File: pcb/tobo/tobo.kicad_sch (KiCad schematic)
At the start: 96 parts, among them J1 Molex 538-54548-2272, J2 Conn_01x02_Pin, J4 Molex 538-54548-2472, J5 Conn_01x09_Pin, J6 Conn_01x09_Pin, J7 Conn_01x09_Pin, J8 Hroparts Elec TYPE-C-31-M-12, U1 TS5A23167, U10 5015, U11 5015, U12 5015, U13 5015, U14 CH340E, U15 5015, U2 ATmega328P-A, U3 TS5A23167, U4 TS5A23167, U5 TS5A23167, U6 5015, U7 5015, U8 5015, U9 5015, X1 TestPoint, X2 TestPoint, X7 TestPoint, Y4 TestPoint

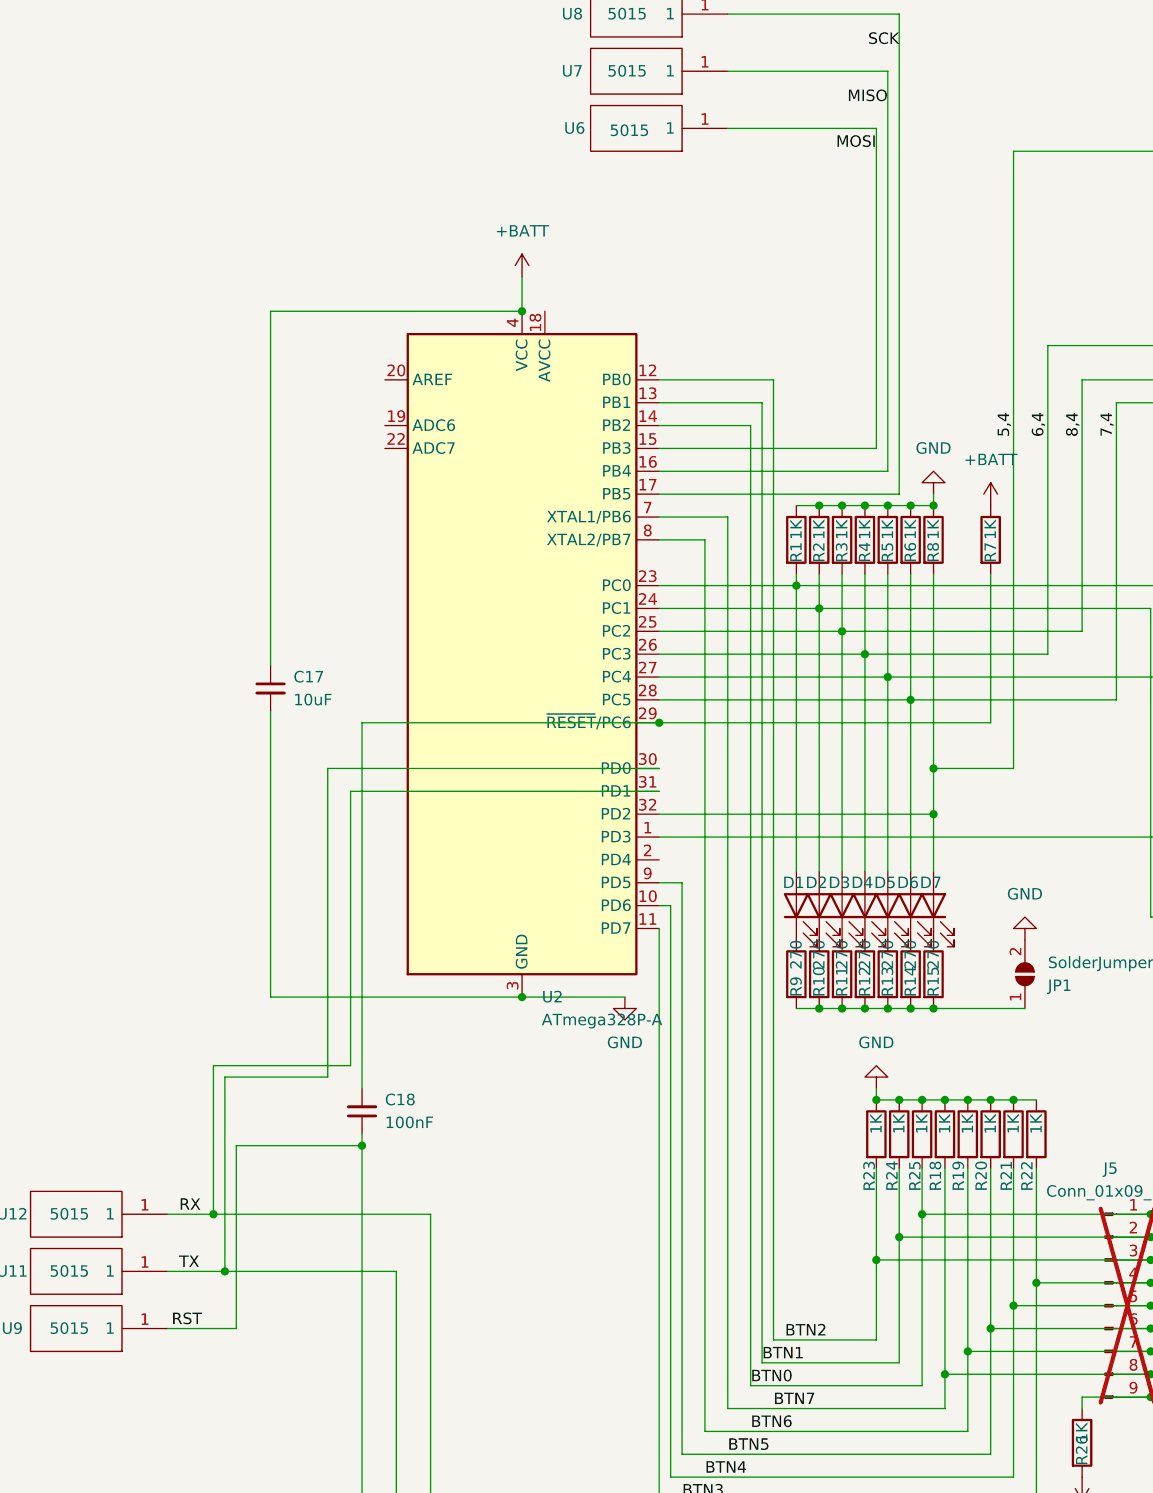
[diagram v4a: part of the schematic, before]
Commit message: Separate DTR from RST pin. They are different.
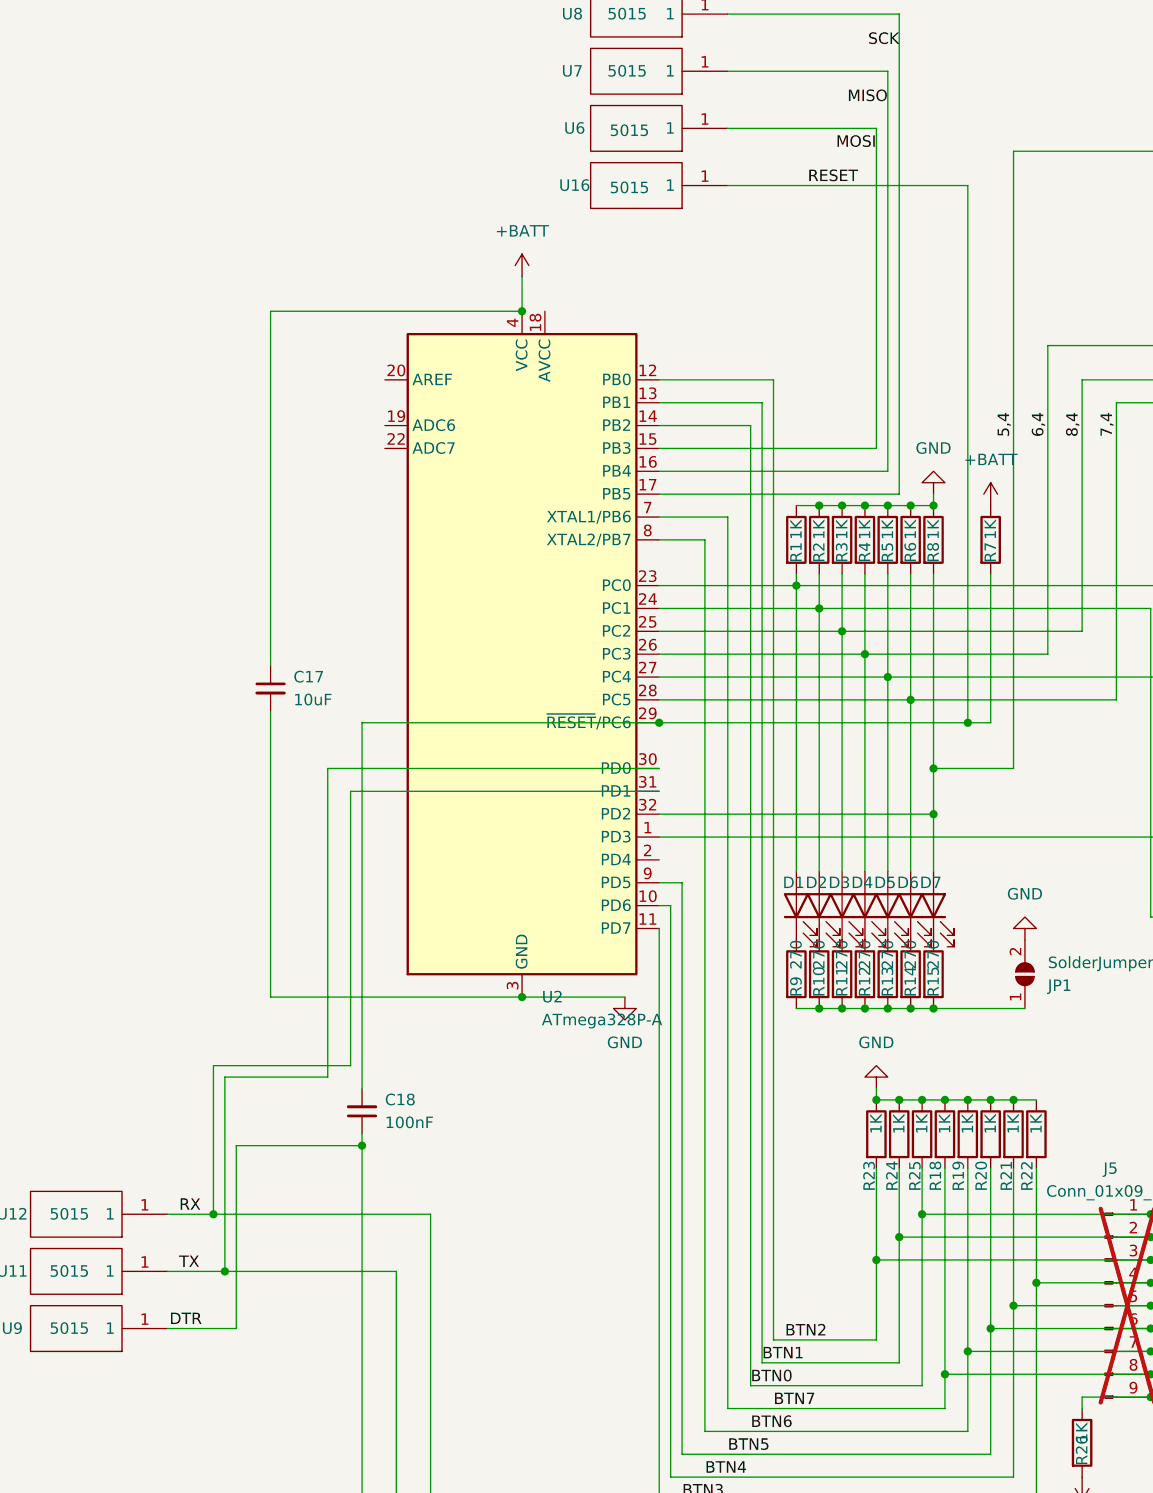
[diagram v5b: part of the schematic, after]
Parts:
- added U16: 5015, tobo-footprints:5015, symbol tobo-components:5015
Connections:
- net RESET: now reaches C18.2, R7.2, U2.29 (~{RESET}/PC6)
- net RESET: now also U16.1
- net RST renamed DTR
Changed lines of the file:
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@@
 	)
 	(junction
+		(at 124.46 110.49)
+		(diameter 0)
+		(color 0 0 0 0)
+	)
+	(junction
 		(at 189.23 81.28)
 		(diameter 0)
@@
 	(wire
 		(pts
+			(xy 124.46 110.49) (xy 124.46 50.8)
+		)
+		(stroke
+			(width 0)
+			(type default)
+		)
+	)
+	(wire
+		(pts
 			(xy 101.6 74.93) (xy 101.6 181.61)
 		)
@@
 	(wire
 		(pts
-			(xy 90.17 110.49) (xy 127 110.49)
+			(xy 90.17 110.49) (xy 124.46 110.49)
 		)
 		(stroke
@@
 	(wire
 		(pts
+			(xy 124.46 110.49) (xy 127 110.49)
+		)
+		(stroke
+			(width 0)
+			(type default)
+		)
+	)
+	(wire
+		(pts
 			(xy 223.52 102.87) (xy 171.45 102.87)
 		)
@@
 	(wire
 		(pts
+			(xy 124.46 50.8) (xy 97.79 50.8)
+		)
+		(stroke
+			(width 0)
+			(type default)
+		)
+	)
+	(wire
+		(pts
 			(xy 115.57 204.47) (xy 111.76 204.47)
 		)
@@
 		)
 	)
-	(label "RST"
+	(label "DTR"
 		(at 39.37 177.8 180)
 		(fields_autoplaced yes)
@@
 		)
 	)
+	(label "RESET"
+		(at 106.68 50.8 0)
+		(fields_autoplaced yes)
+		(effects
+			(font
+				(size 1.27 1.27)
+			)
+			(justify left bottom)
+		)
+	)
 	(label "RX"
 		(at 36.83 165.1 0)
@@
 					(unit 1)
 				)
+			)
+		)
+	)
+	(symbol
+		(lib_id "tobo-components:5015")
+		(at 97.79 50.8 180)
+		(unit 1)
+		(exclude_from_sim no)
+		(in_bom yes)
+		(on_board yes)
+		(dnp no)
+		(property "Reference" "U16"
+			(at 80.772 50.8 0)
+			(effects
+				(font
+					(size 1.27 1.27)
+				)
+			)
+		)
+		(property "Value" "5015"
+			(at 86.868 51.054 0)
+			(effects
+				(font
+					(size 1.27 1.27)
+				)
+			)
+		)
+		(property "Footprint" "tobo-footprints:5015"
+			(at 81.28 53.34 0)
+			(effects
+				(font
+					(size 1.27 1.27)
+				)
+				(justify left)
+				(hide yes)
+			)
+		)
+		(property "Datasheet" "http://www.keyelco.com/product-pdf.cfm?p=1353"
+			(at 81.28 50.8 0)
+			(effects
+				(font
+					(size 1.27 1.27)
+				)
+				(justify left)
+				(hide yes)
+			)
+		)
+		(property "Description" "Conn Test Point 1 POS Solder ST SMD 1 Port T/R"
+			(at 81.28 48.26 0)
+			(effects
+				(font
+					(size 1.27 1.27)
+				)
+				(justify left)
+				(hide yes)
+			)
+		)
+		(property "Height" "1.52"
+			(at 81.28 45.72 0)
+			(effects
+				(font
+					(size 1.27 1.27)
+				)
+				(justify left)
+				(hide yes)
+			)
+		)
+		(property "Manufacturer_Name" "Keystone Electronics"
+			(at 81.28 43.18 0)
+			(effects
+				(font
+					(size 1.27 1.27)
+				)
+				(justify left)
+				(hide yes)
+			)
+		)
+		(property "Manufacturer_Part_Number" "5015"
+			(at 81.28 40.64 0)
+			(effects
+				(font
+					(size 1.27 1.27)
+				)
+				(justify left)
+				(hide yes)
+			)
+		)
+		(property "Mouser Part Number" "534-5015"
+			(at 81.28 38.1 0)
+			(effects
+				(font
+					(size 1.27 1.27)
+				)
+				(justify left)
+				(hide yes)
+			)
+		)
+		(property "Mouser Price/Stock" "https://www.mouser.co.uk/ProductDetail/Keystone-Electronics/5015?qs=qOqV1E1P08ShW56PtUq2FA%3D%3D"
+			(at 81.28 35.56 0)
+			(effects
+				(font
+					(size 1.27 1.27)
+				)
+				(justify left)
+				(hide yes)
+			)
+		)
+		(property "Arrow Part Number" "5015"
+			(at 81.28 33.02 0)
+			(effects
+				(font
+					(size 1.27 1.27)
+				)
+				(justify left)
+				(hide yes)
+			)
+		)
+		(property "Arrow Price/Stock" "https://www.arrow.com/en/products/5015/keystone-electronics?utm_currency=USD&region=europe"
+			(at 81.28 30.48 0)
+			(effects
+				(font
+					(size 1.27 1.27)
+				)
+				(justify left)
+				(hide yes)
+			)
+		)
+		(pin "1"
+		)
+		(instances
+			(project "tobo"
+				(path "/ce2fc4a9-618f-4cc1-898a-224ffa79d770"
+					(reference "U16")
+					(unit 1)
+				)

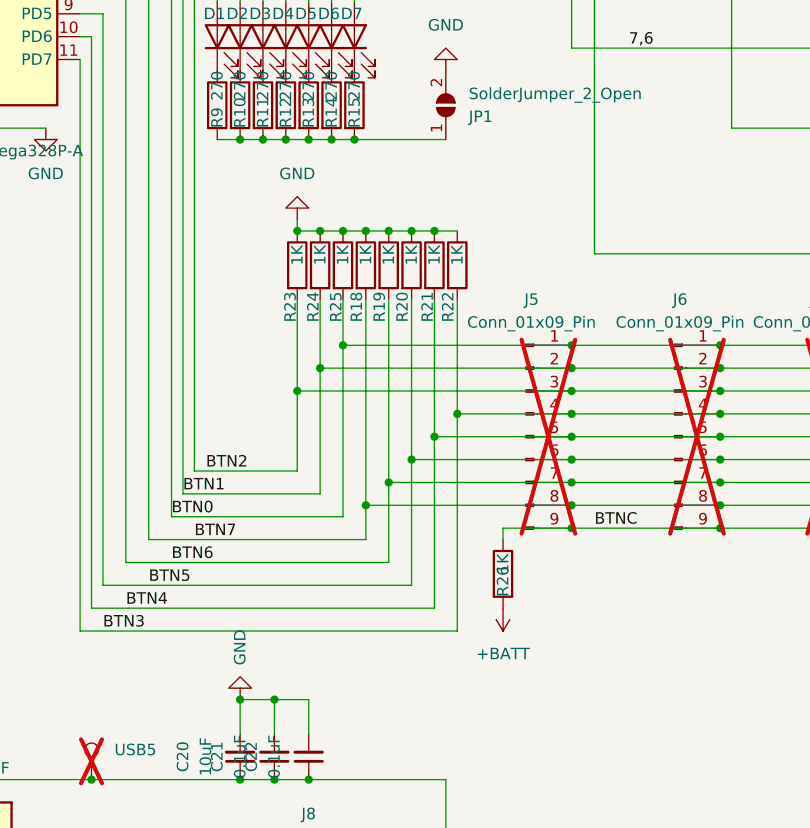
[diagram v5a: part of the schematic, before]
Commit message: Internal pull-ups for the buttons. May as well.
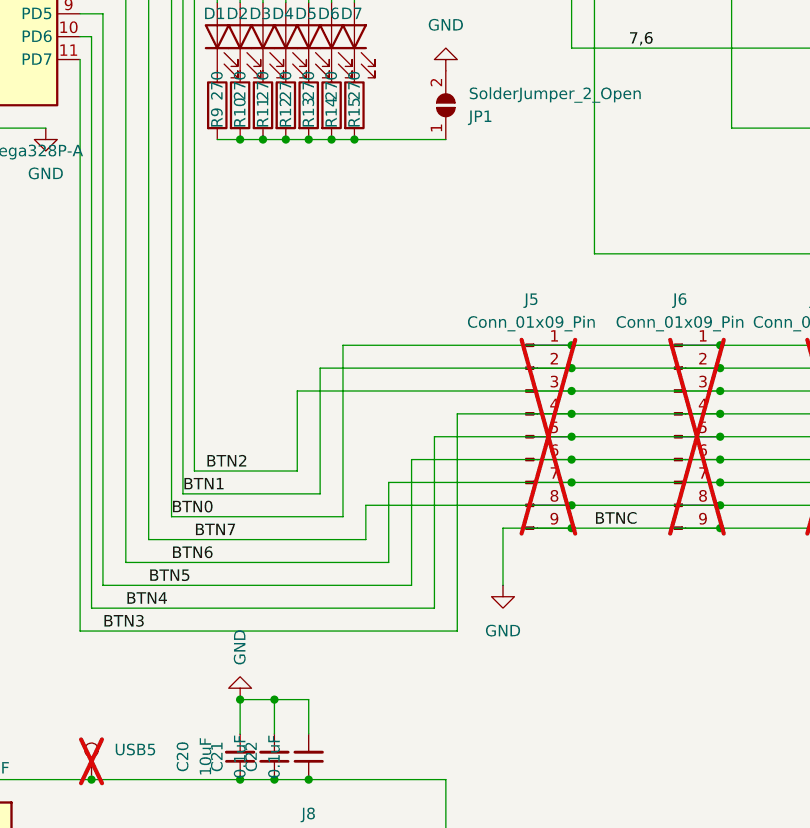
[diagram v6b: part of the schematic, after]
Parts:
- removed R18, R19, R20, R21, R22, R23, R24, R25, R26: 1K, Resistor_SMD:R_0201_0603Metric, symbol Device:R
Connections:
- net BTNC is gone; now on net GND: J5.9 (Pin_9), J6.9 (Pin_9), J7.9 (Pin_9), S1.1 (COM_1), S1.3 (COM_2), S2.1 (COM_1), S2.3 (COM_2), S3.1 (COM_1), S3.3 (COM_2), S4.1 (COM_1), S4.3 (COM_2), S5.1 (COM_1), S5.3 (COM_2)

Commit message: PCB and documentation tweaks
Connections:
- net X1: now reaches J1.11 (X1)
- net X1: now also C7.2, C8.1, J4.13 (X1)
- net X2: now reaches J1.12 (X2)
- net X2: now also C13.1, C14.1, C5.1, C6.2, C9.2, J4.14 (X2), U4.2 (COM1), U4.6 (COM2), U5.6 (COM2), X7.1
- net X3: now reaches J1.13 (X3)
- net X3: now also C1.2, C2.1, J4.15 (X3)
- net X4: now reaches J1.14 (X4)
- net X4: now also C3.1, C4.2, J4.16 (X4), X1.1
- net 5,4 renamed 3,4
- net 6,4 renamed 4,4
- net 7,4 renamed 2,4
- net 7,5 renamed 2,5
- net 7,6 renamed 2,6
- net 7,7 renamed 2,7
- net 8,4 renamed 1,4
- removed net X5: C1.2, C2.1, J1.17 (X5), J4.19 (X5)
- removed net X6: C3.1, C4.2, J1.18 (X6), J4.20 (X6), X1.1
- removed net X7: C13.1, C14.1, C5.1, C6.2, C9.2, J1.16 (X7), J4.18 (X7), U4.2 (COM1), U4.6 (COM2), U5.6 (COM2), X7.1
- removed net X8: C7.2, C8.1, J1.15 (X8), J4.17 (X8)
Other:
- moved on the sheet: X1

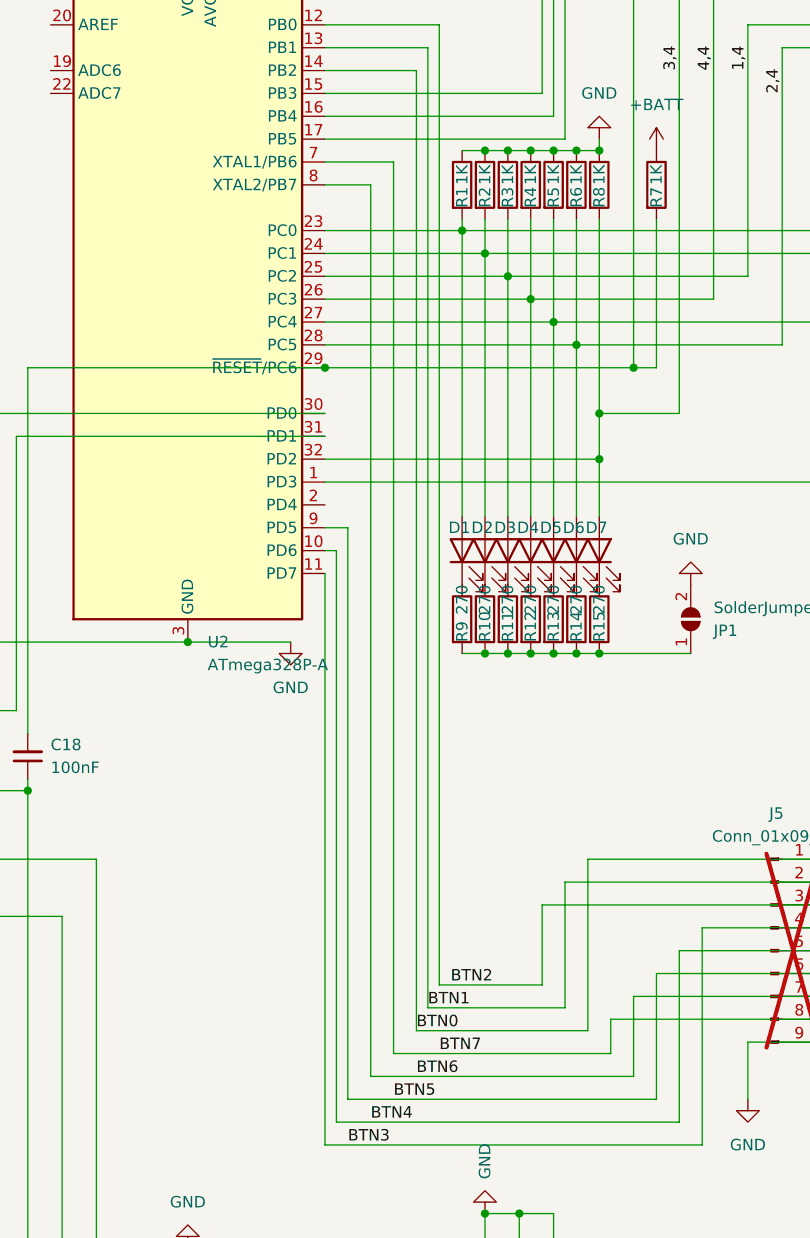
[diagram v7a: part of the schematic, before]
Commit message: Swapped some GPIO to avoid PCINT problems
This lead to a tasty basket weave of traces under the MCU, but that's
fine I guess.

The only reason this change was "necessary" is because regular arduino
doesn't expose gpio on the crystal pins. Therefore the PCINT libraries
don't seem to support enabling the pin change interrupt on those pins.

It was neat to have them as buttons, from a routing perspective, but
this should -work- which seems more important.
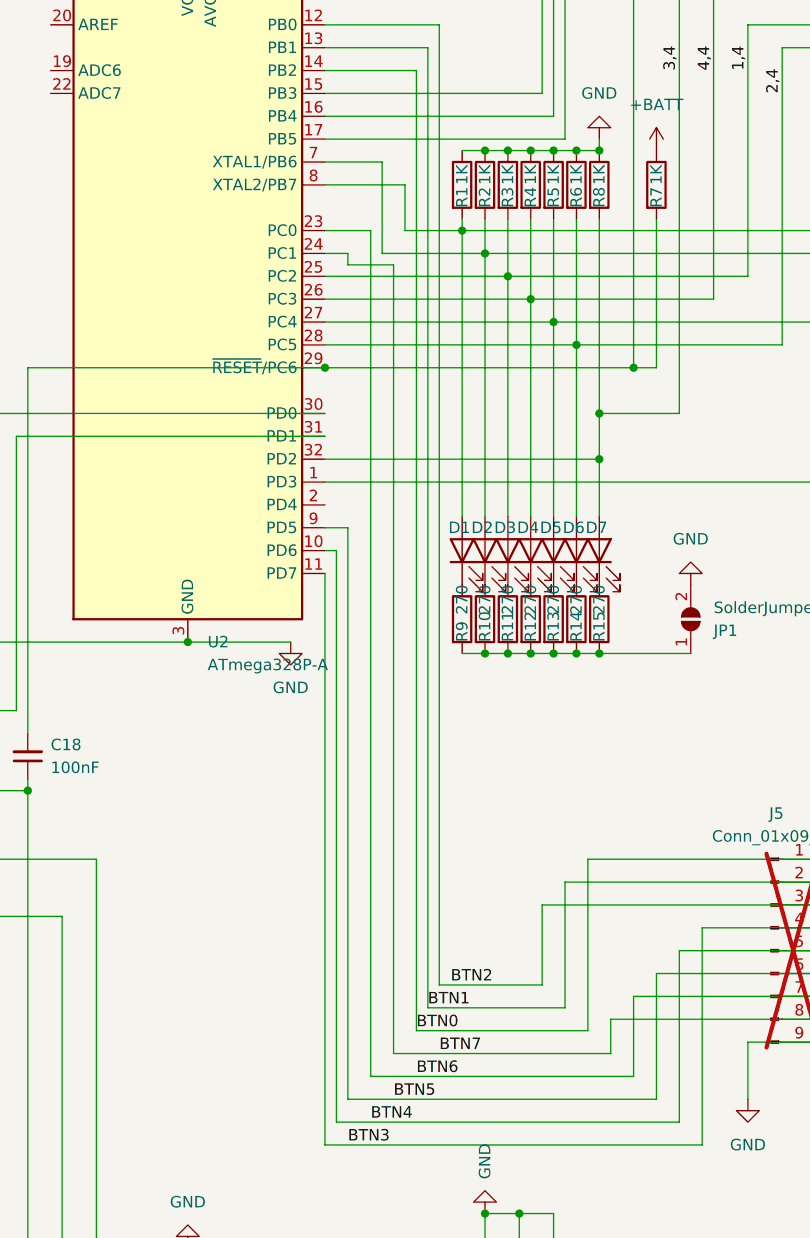
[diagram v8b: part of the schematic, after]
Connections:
- net 2,6: now also U2.7 (XTAL1/PB6); no longer U2.24 (PC1)
- net 2,7: now also U2.8 (XTAL2/PB7); no longer U2.23 (PC0)
- net BTN6: now also U2.23 (PC0); no longer U2.8 (XTAL2/PB7)
- net BTN7: now also U2.24 (PC1); no longer U2.7 (XTAL1/PB6)
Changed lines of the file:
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@@
-	(wire
-		(pts
-			(xy 95.25 90.17) (xy 95.25 189.23)
-		)
-		(stroke
-			(width 0)
-			(type default)
-		)
-	)
 	(wire
 		(pts
@@
 	(wire
 		(pts
+			(xy 90.17 97.79) (xy 92.71 97.79)
+		)
+		(stroke
+			(width 0)
+			(type default)
+		)
+	)
+	(wire
+		(pts
 			(xy 189.23 144.78) (xy 177.8 144.78)
 		)
@@
 	(wire
 		(pts
+			(xy 92.71 99.06) (xy 97.79 99.06)
+		)
+		(stroke
+			(width 0)
+			(type default)
+		)
+	)
+	(wire
+		(pts
 			(xy 254 96.52) (xy 247.65 96.52)
 		)
@@
 	(wire
 		(pts
-			(xy 107.95 97.79) (xy 90.17 97.79)
-		)
-		(stroke
-			(width 0)
-			(type default)
-		)
-	)
-	(wire
-		(pts
 			(xy 113.03 102.87) (xy 113.03 127)
 		)
@@
 	(wire
 		(pts
+			(xy 99.06 90.17) (xy 90.17 90.17)
+		)
+		(stroke
+			(width 0)
+			(type default)
+		)
+	)
+	(wire
+		(pts
 			(xy 195.58 81.28) (xy 196.85 81.28)
 		)
@@
 	(wire
 		(pts
-			(xy 90.17 90.17) (xy 95.25 90.17)
-		)
-		(stroke
-			(width 0)
-			(type default)
-		)
-	)
-	(wire
-		(pts
 			(xy 127 177.8) (xy 144.78 177.8)
 		)
@@
 	(wire
 		(pts
+			(xy 90.17 95.25) (xy 95.25 95.25)
+		)
+		(stroke
+			(width 0)
+			(type default)
+		)
+	)
+	(wire
+		(pts
+			(xy 96.52 97.79) (xy 96.52 87.63)
+		)
+		(stroke
+			(width 0)
+			(type default)
+		)
+	)
+	(wire
+		(pts
 			(xy 91.44 130.81) (xy 91.44 194.31)
 		)
@@
 	(wire
 		(pts
-			(xy 90.17 87.63) (xy 97.79 87.63)
+			(xy 90.17 87.63) (xy 96.52 87.63)
 		)
 		(stroke
@@
 	(wire
 		(pts
+			(xy 107.95 97.79) (xy 96.52 97.79)
+		)
+		(stroke
+			(width 0)
+			(type default)
+		)
+	)
+	(wire
+		(pts
+			(xy 97.79 99.06) (xy 97.79 186.69)
+		)
+		(stroke
+			(width 0)
+			(type default)
+		)
+	)
+	(wire
+		(pts
 			(xy 254 97.79) (xy 251.46 97.79)
 		)
@@
 	(wire
 		(pts
+			(xy 92.71 97.79) (xy 92.71 99.06)
+		)
+		(stroke
+			(width 0)
+			(type default)
+		)
+	)
+	(wire
+		(pts
 			(xy 118.11 142.24) (xy 120.65 142.24)
 		)
@@
 	(wire
 		(pts
-			(xy 90.17 95.25) (xy 105.41 95.25)
-		)
-		(stroke
-			(width 0)
-			(type default)
-		)
-	)
-	(wire
-		(pts
 			(xy 222.25 116.84) (xy 222.25 129.54)
 		)
@@
 	(wire
 		(pts
+			(xy 95.25 95.25) (xy 95.25 189.23)
+		)
+		(stroke
+			(width 0)
+			(type default)
+		)
+	)
+	(wire
+		(pts
 			(xy 298.45 213.36) (xy 328.93 213.36)
 		)
@@
 	(wire
 		(pts
-			(xy 97.79 87.63) (xy 97.79 186.69)
-		)
-		(stroke
-			(width 0)
-			(type default)
-		)
-	)
-	(wire
-		(pts
 			(xy 210.82 154.94) (xy 209.55 154.94)
 		)
@@
 	(wire
 		(pts
+			(xy 105.41 95.25) (xy 99.06 95.25)
+		)
+		(stroke
+			(width 0)
+			(type default)
+		)
+	)
+	(wire
+		(pts
 			(xy 162.56 123.19) (xy 162.56 140.97)
 		)
@@
 		)
 		(stroke
+			(width 0)
+			(type default)
+		)
+	)
+	(wire
+		(pts
+			(xy 99.06 95.25) (xy 99.06 90.17)
+		)
+		(stroke
